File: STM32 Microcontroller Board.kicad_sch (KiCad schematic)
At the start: 0 parts

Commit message: Your descriptive message here
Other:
- sheet GPIO extension renamed Power
- sheet Power: file GPIO_extension.kicad_sch -> Power.kicad_sch
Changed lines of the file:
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@@
 			(color 0 0 0 0.0000)
 		)
-		(property "Sheetname" "GPIO extension"
+		(property "Sheetname" "Power"
 			(at 117.094 124.0024 0)
 			(effects
@@
 			)
 		)
-		(property "Sheetfile" "GPIO_extension.kicad_sch"
+		(property "Sheetfile" "Power.kicad_sch"
 			(at 117.094 151.7146 0)
 			(effects

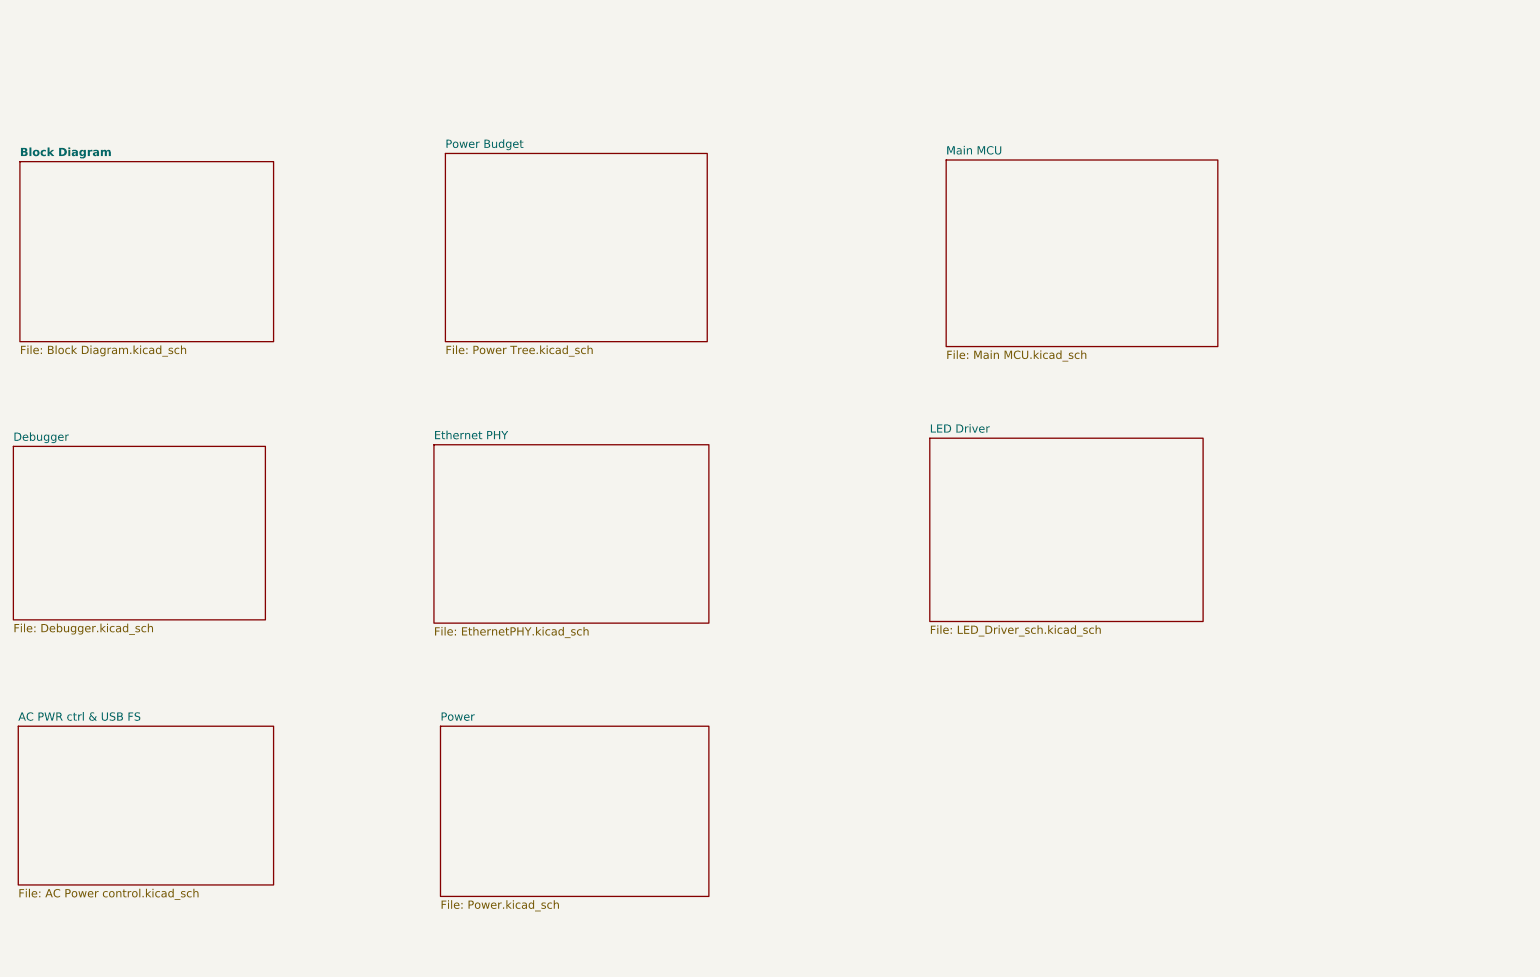
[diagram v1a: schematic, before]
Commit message: Updated the root schematic page
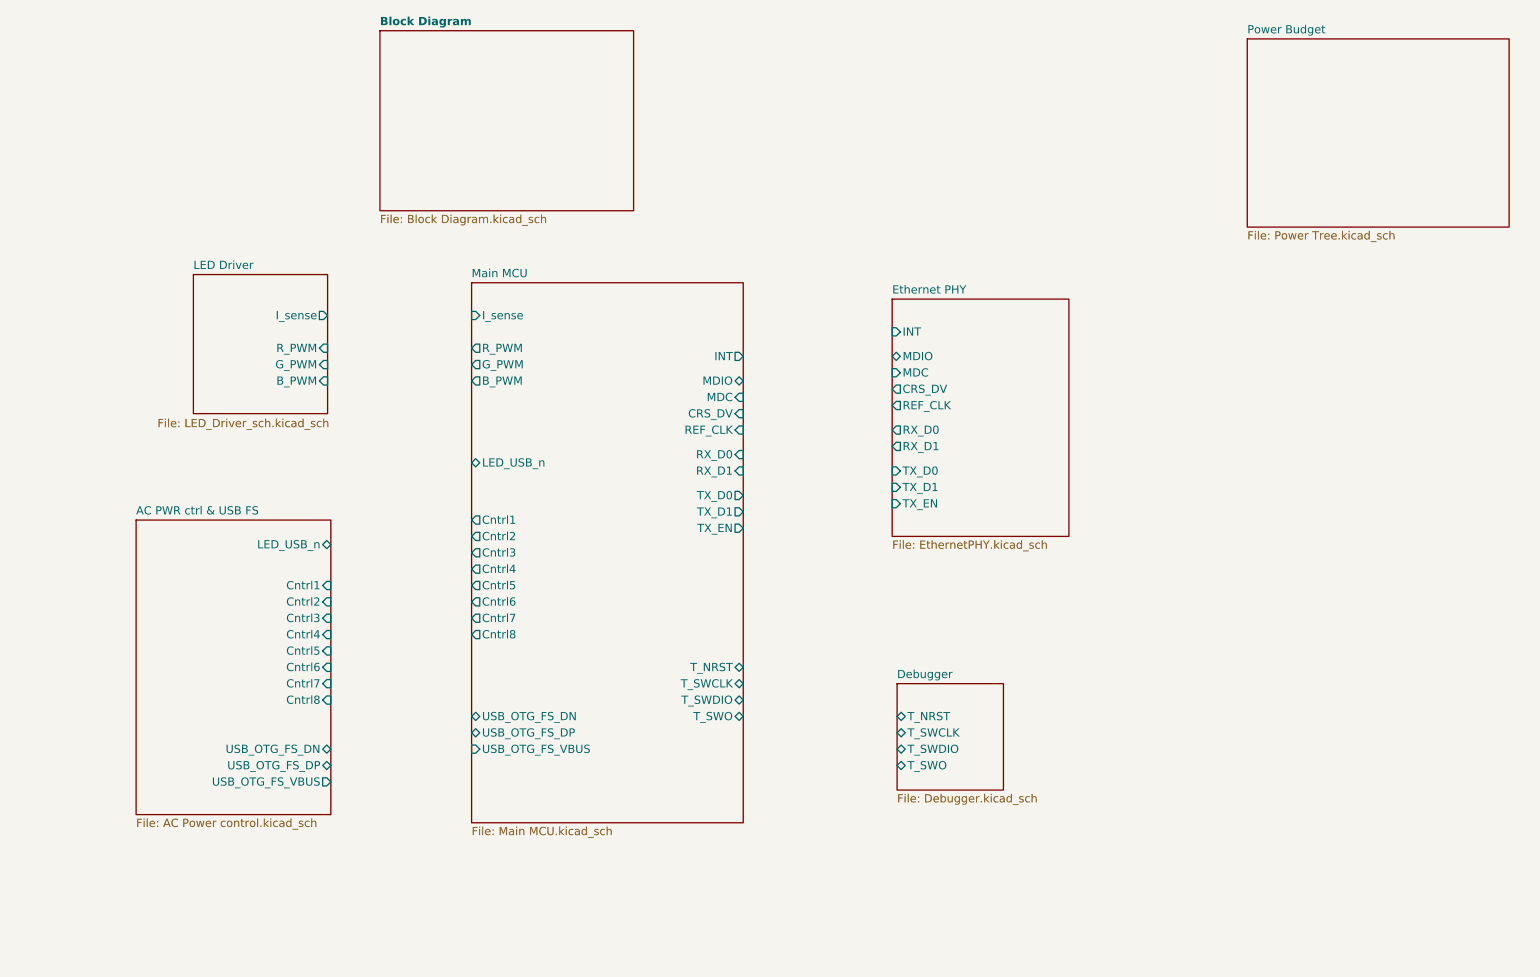
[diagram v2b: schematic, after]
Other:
- removed sheet Power
- sheet AC PWR ctrl & USB FS ports: added Cntrl1, Cntrl2, Cntrl3, Cntrl4, Cntrl5, Cntrl6, Cntrl7, Cntrl8, LED_USB_n, USB_OTG_FS_DN, USB_OTG_FS_DP, USB_OTG_FS_VBUS; removed none
- sheet Debugger ports: added T_NRST, T_SWCLK, T_SWDIO, T_SWO; removed none
- sheet Ethernet PHY ports: added CRS_DV, INT, MDC, MDIO, REF_CLK, RX_D0, RX_D1, TX_D0, TX_D1, TX_EN; removed none
- sheet LED Driver ports: added B_PWM, G_PWM, I_sense, R_PWM; removed none
- sheet Main MCU ports: added B_PWM, CRS_DV, Cntrl1, Cntrl2, Cntrl3, Cntrl4, Cntrl5, Cntrl6, Cntrl7, Cntrl8, G_PWM, INT, I_sense, LED_USB_n, MDC, MDIO, REF_CLK, RX_D0, RX_D1, R_PWM, TX_D0, TX_D1, TX_EN, T_NRST, T_SWCLK, T_SWDIO, T_SWO, USB_OTG_FS_DN, USB_OTG_FS_DP, USB_OTG_FS_VBUS; removed none

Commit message: Done ERC + Documentation
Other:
- sheet Debugger ports: added RESET; removed T_NRST
- sheet Main MCU ports: added RESET; removed T_NRST
- note added: "For reference only"

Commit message: Initial Review Changes
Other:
- company: (none) -> _electronic_projects
- title: (none) -> DeskNode-F4
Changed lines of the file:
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@@
 	(generator_version "9.0")
 	(paper "A4")
+	(title_block
+		(title "DeskNode-F4")
+		(rev "A")
+		(company "_electronic_projects")
+		(comment 1 "Wajahatulla Sharif")
+		(comment 2 "Designed by ")
+	)
 	(rectangle
 		(start 245.618 145.034)

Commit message: Layout placement
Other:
- sheet Debugger ports: added RX, TX; removed none
- sheet Main MCU ports: added RX, TX; removed none
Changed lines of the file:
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@@
+	(wire
+		(pts
+			(xy 163.83 135.89) (xy 187.96 135.89)
+		)
+		(stroke
+			(width 0)
+			(type default)
+		)
+	)
 	(wire
 		(pts
@@
 		(pts
 			(xy 163.83 67.31) (xy 187.96 67.31)
+		)
+		(stroke
+			(width 0)
+			(type default)
+		)
+	)
+	(wire
+		(pts
+			(xy 163.83 133.35) (xy 187.96 133.35)
 		)
 		(stroke
@@
 	)
 	(sheet
-		(at 187.96 118.11)
-		(size 16.51 16.51)
+		(at 187.96 119.634)
+		(size 16.51 18.796)
 		(exclude_from_sim no)
 		(in_bom yes)
@@
 		)
 		(property "Sheetname" "Debugger"
-			(at 187.96 117.3984 0)
+			(at 187.96 118.9224 0)
 			(effects
 				(font
@@
 		)
 		(property "Sheetfile" "Debugger.kicad_sch"
-			(at 187.96 135.2046 0)
+			(at 187.96 139.0146 0)
 			(effects
 				(font
@@
 		(pin "T_SWO" bidirectional
 			(at 187.96 130.81 180)
+			(effects
+				(font
+					(size 1.27 1.27)
+				)
+				(justify left)
+			)
+		)
+		(pin "RX" bidirectional
+			(at 187.96 133.35 180)
+			(effects
+				(font
+					(size 1.27 1.27)
+				)
+				(justify left)
+			)
+		)
+		(pin "TX" bidirectional
+			(at 187.96 135.89 180)
 			(effects
 				(font
@@
 			)
 		)
+		(pin "RX" bidirectional
+			(at 163.83 135.89 0)
+			(effects
+				(font
+					(size 1.27 1.27)
+				)
+				(justify right)
+			)
+		)
+		(pin "TX" bidirectional
+			(at 163.83 133.35 0)
+			(effects
+				(font
+					(size 1.27 1.27)
+				)
+				(justify right)
+			)
+		)

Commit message: Layout Routing
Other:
- sheet LED Driver ports: added V_sense; removed none
- sheet Main MCU ports: added V_sense; removed none
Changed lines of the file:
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@@
+	(wire
+		(pts
+			(xy 99.06 63.5) (xy 121.92 63.5)
+		)
+		(stroke
+			(width 0)
+			(type default)
+		)
+	)
 	(wire
 		(pts
@@
 		(pin "R_PWM" input
 			(at 99.06 66.04 0)
+			(effects
+				(font
+					(size 1.27 1.27)
+				)
+				(justify right)
+			)
+		)
+		(pin "V_sense" output
+			(at 99.06 63.5 0)
 			(effects
 				(font
@@
 			)
 		)
+		(pin "V_sense" input
+			(at 121.92 63.5 180)
+			(effects
+				(font
+					(size 1.27 1.27)
+				)
+				(justify left)
+			)
+		)

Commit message: Review files
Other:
- company: _electronic_projects -> (none)
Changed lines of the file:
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@@
 		(title "DeskNode-F4")
 		(rev "A")
-		(company "_electronic_projects")
-		(comment 1 "Wajahatulla Sharif")
-		(comment 2 "Designed by ")
 	)
 	(rectangle
